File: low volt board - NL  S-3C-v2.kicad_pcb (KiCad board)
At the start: 2 copper layers, 152.4 x 78.7 mm, 42 parts, among them J1 ESP32-S3-ETH-WAVETREE-Footpri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, J2 ILI9341 TFT 2.8" Display with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, J3 4 Channel 5v Relay Connector, J4 SPDT (on)-off-(on), J5 ADC Inputs - 24v side, J6 Dry Contact OptoCoupler, J8 5vIn, Q1-Buzzer1 S8050, SW1 SW_SPDT, U1 ADS1115IDGS - low volt, U2 ADS1115IDGS - 24v, U3-Opto1 PC817

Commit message: Final design before first autoroute
Co-Authored-By: Claude Opus 4.6 <noreply@anthropic.com>
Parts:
- moved J3 38.4 mm to (155.0, 67.0), turned to 90 degrees
- moved J8 37.2 mm to (132.7, 53.3), turned to 90 degrees
- moved J5 27.9 mm to (155.0, 104.0)
- moved R17-A1-3 23.1 mm to (142.8, 78.6)
- moved R18-A1-2 23.0 mm to (142.8, 83.7)
- moved R10-A2-3 22.5 mm to (142.8, 88.7)
- moved R16-A2-0 22.5 mm to (142.8, 104.0)
- moved R8-A2-1 22.5 mm to (142.8, 98.9)
- moved R9-A2-2 22.5 mm to (142.8, 93.8)
- moved R2-Throw-A1 21.2 mm to (89.8, 78.8)
- moved R4-Common1 20.9 mm to (89.8, 73.8)
- moved J4 20.9 mm to (76.8, 78.8)
- moved R3-ThrowB1 20.5 mm to (89.8, 68.7)
- moved R15-Purple1 17.5 mm to (137.6, 101.6)
- moved SW1 17.0 mm to (88.9, 58.4), turned to 90 degrees
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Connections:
- net /IO21 renamed /Buzer-IO21
- net Net-(LS1-Buzzer1--LEAD) renamed /Buzzer-3
- net Net-(Q1-Buzzer1-B) renamed /Buzzer-2
- J3 pad 1: +5V -> /IO3
- J3 pad 2: GND -> /IO15
- J3 pad 3: /IO16 -> /IO18
- J3 pad 4: /IO18 -> /IO16
- J3 pad 5: /IO15 -> GND
- J3 pad 6: /IO3 -> +5V
- J5 pad 6: /A1-2-E -> /A1-3-E
- J8 pad 1: +5V -> GND
- J8 pad 2: GND -> +5V
- R8-A2-1 pad 1: /A2-1 -> /A2-1-E
- R8-A2-1 pad 2: /A2-1-E -> /A2-1
- R9-A2-2 pad 1: /A2-2 -> /A2-2-E
- R9-A2-2 pad 2: /A2-2-E -> /A2-2
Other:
- board size 152.4 x 78.7 mm -> 124.5 x 73.7 mm

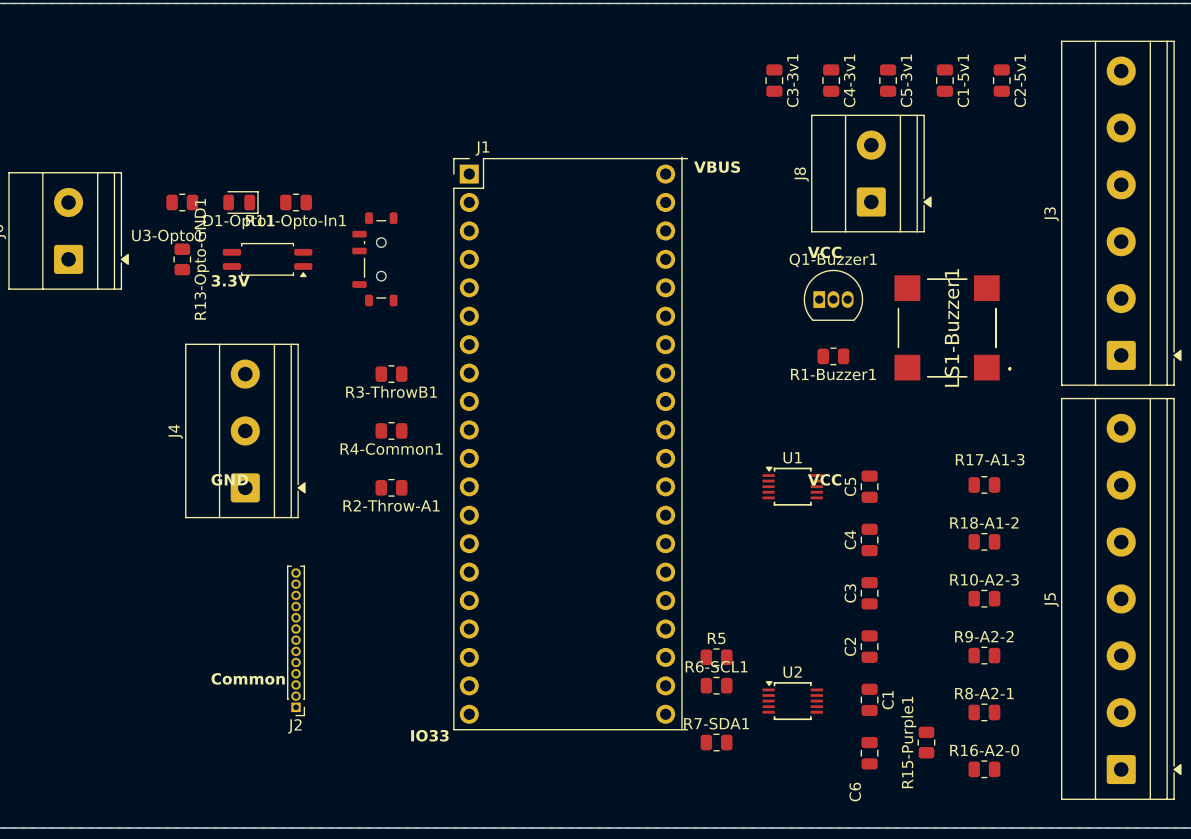
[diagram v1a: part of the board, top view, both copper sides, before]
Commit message: First routing done
Co-Authored-By: Claude Opus 4.6 <noreply@anthropic.com>
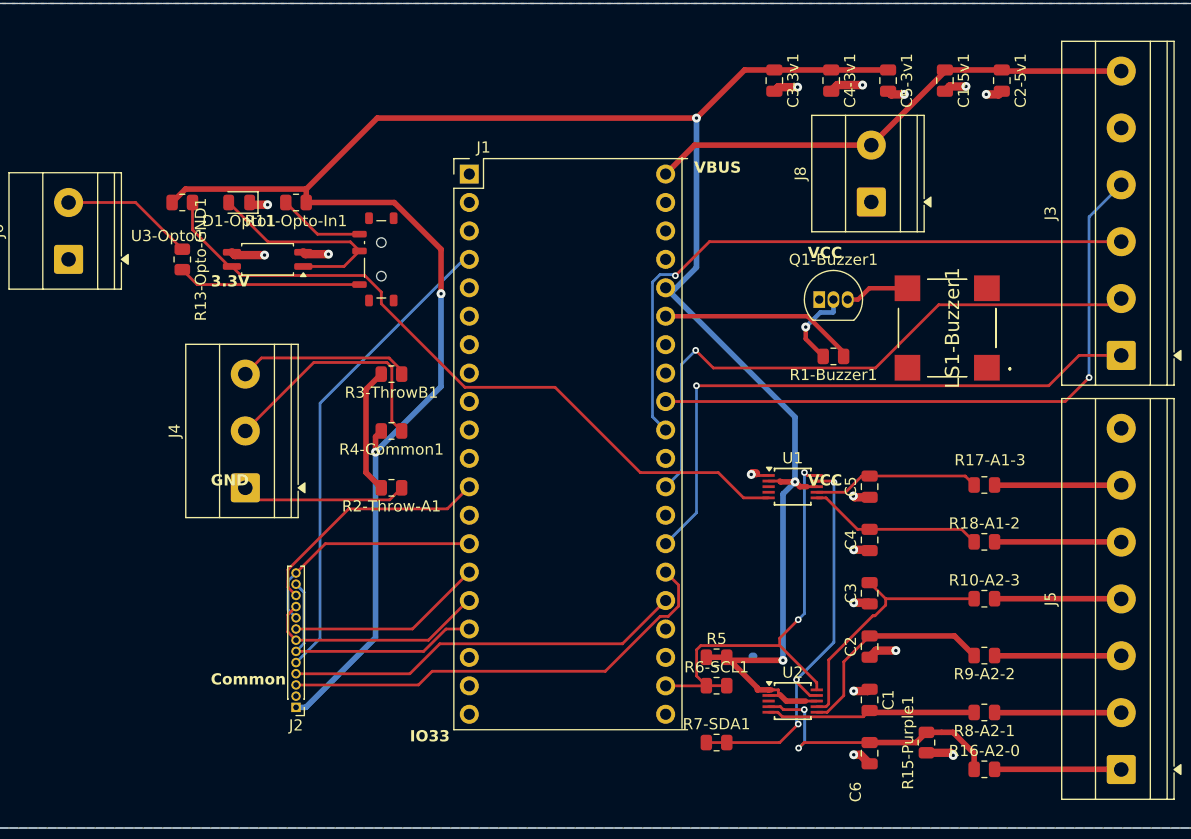
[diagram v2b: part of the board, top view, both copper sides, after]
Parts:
- turned R8-A2-1 to 180 degrees
- turned R9-A2-2 to 180 degrees
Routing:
- net +3.3V: track 0.00 -> 210.3 mm, vias 0 -> 5
- net /A1-1: track 0.00 -> 64.4 mm
- net /IO18: track 0.00 -> 57.1 mm, vias 0 -> 1
- net /IO16: track 0.00 -> 57.1 mm, vias 0 -> 1
- net /IO15: track 0.00 -> 54.5 mm, vias 0 -> 1
- net /IO3: track 0.00 -> 54.3 mm, vias 0 -> 1
- net +5V: track 0.00 -> 44.7 mm
- net /IO48: track 0.00 -> 42.7 mm
- net /IO2: track 0.00 -> 40.6 mm
- net /SCL: track 0.00 -> 39.5 mm, vias 0 -> 2
- net /SDA: track 0.00 -> 36.0 mm, vias 0 -> 3
- net /IO1: track 0.00 -> 35.7 mm
- net GND: track 0.00 -> 31.9 mm, vias 0 -> 16
- net /A2-0: track 0.00 -> 25.4 mm, vias 0 -> 2
- net /IO35: track 0.00 -> 22.9 mm
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
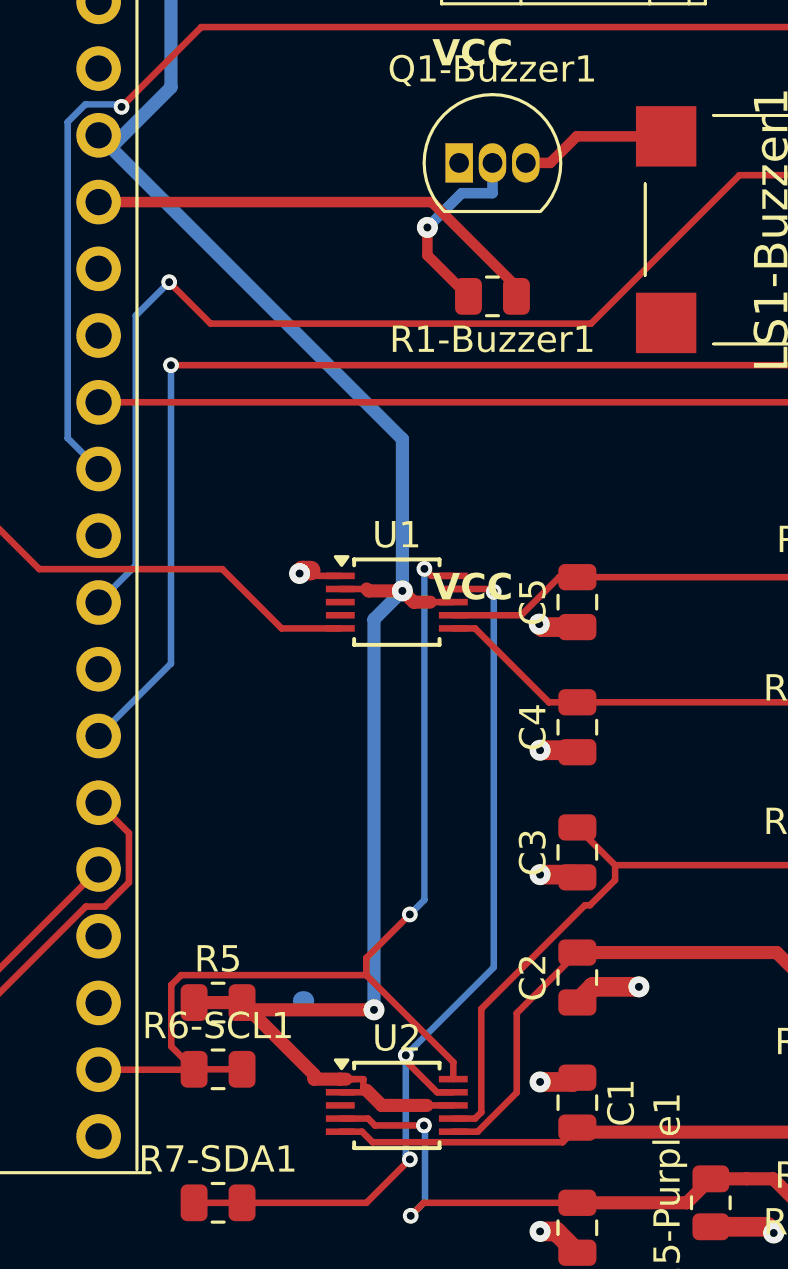
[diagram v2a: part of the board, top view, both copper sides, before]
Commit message: Traces and DRC passing - still need mounting holes
Co-Authored-By: Claude Opus 4.6 <noreply@anthropic.com>
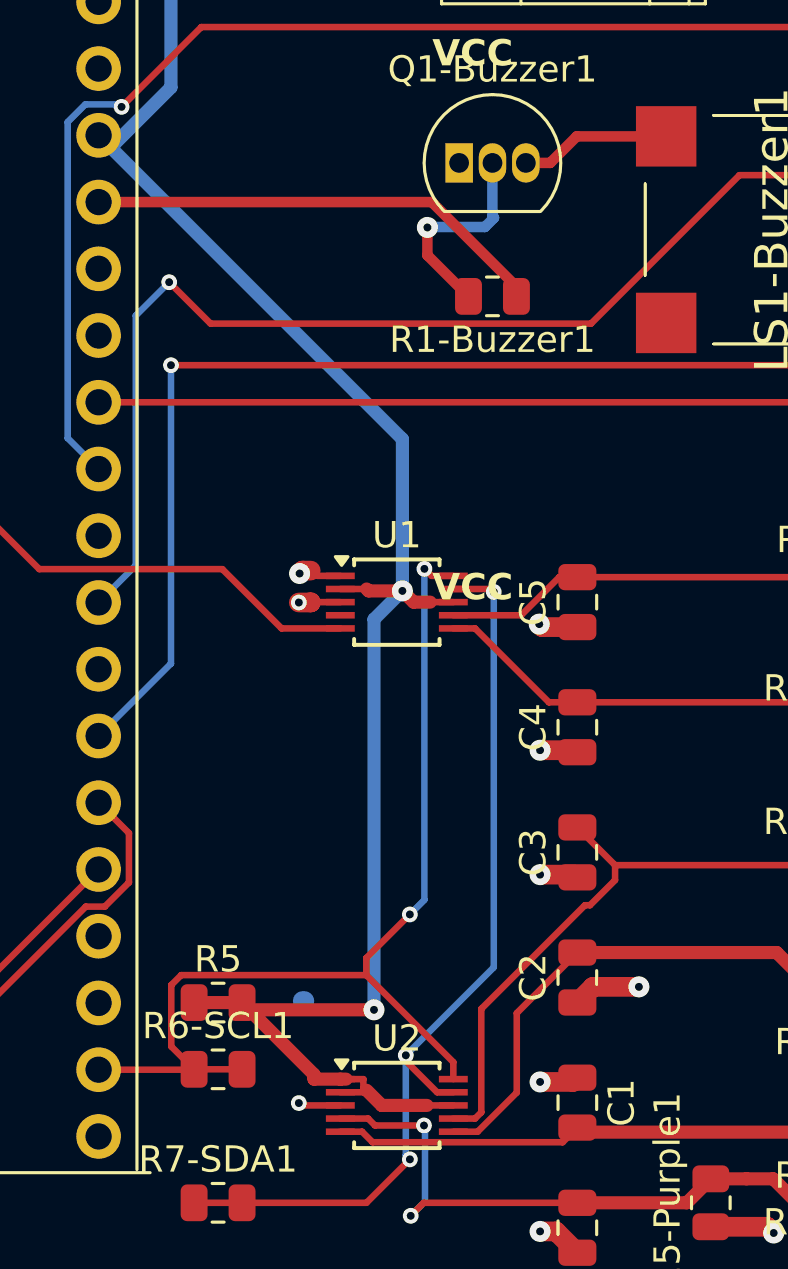
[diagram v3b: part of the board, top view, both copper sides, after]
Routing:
- net GND: track 31.9 -> 35.1 mm, vias 16 -> 18
- net /Buzzer-2: track 7.44 -> 8.07 mm
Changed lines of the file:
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@@
 		(sheetname "/")
 		(sheetfile "low volt board - NL  S-3C-v2.kicad_sch")
+		(clearance 0.15)
 		(attr through_hole)
 		(fp_line
@@
 	)
 	(segment
+		(start 122.374 78.74)
+		(end 122.374 78.726)
+		(width 0.75)
+		(layer "F.Cu")
+		(net 2)
+	)
+	(segment
 		(start 122.0606 77.5258)
 		(end 122.3731 77.5258)
@@
 	)
 	(segment
+		(start 121.92 78.74)
+		(end 122.374 78.74)
+		(width 0.75)
+		(layer "F.Cu")
+		(net 2)
+	)
+	(segment
 		(start 77.3376 53.5401)
 		(end 77.1375 53.34)
@@
 	)
 	(segment
+		(start 122.374 78.726)
+		(end 123.5 78.726)
+		(width 0.25)
+		(layer "F.Cu")
+		(net 2)
+	)
+	(segment
 		(start 141.1295 42.9741)
 		(end 139.6759 42.9741)
@@
 	)
 	(segment
+		(start 121.92 97.79)
+		(end 122.0097 97.8797)
+		(width 0.25)
+		(layer "F.Cu")
+		(net 2)
+	)
+	(segment
+		(start 122.0097 97.8797)
+		(end 123.5 97.8797)
+		(width 0.25)
+		(layer "F.Cu")
+		(net 2)
+	)
+	(segment
 		(start 139.7485 102.4985)
 		(end 137.6 102.4985)
@@
 	)
 	(via
+		(at 121.92 78.74)
+		(size 0.6)
+		(drill 0.3)
+		(layers "F.Cu" "B.Cu")
+		(free yes)
+		(net 2)
+	)
+	(via
 		(at 131.1023 96.9863)
 		(size 0.8)
@@
 	)
 	(via
+		(at 121.92 97.79)
+		(size 0.6)
+		(drill 0.3)
+		(layers "F.Cu" "B.Cu")
+		(free yes)
+		(net 2)
+	)
+	(via
 		(at 131.07 79.5635)
 		(size 0.8)
@@
 	)
 	(segment
-		(start 129.29 62.01)
-		(end 129.29 63.1617)
+		(start 126.8295 64.45)
+		(end 126.8134 64.4661)
 		(width 0.4)
 		(layer "B.Cu")
@@
 	)
 	(segment
-		(start 129.29 63.1617)
-		(end 128.1178 63.1617)
+		(start 129.35 64.1)
+		(end 129 64.45)
 		(width 0.4)
 		(layer "B.Cu")
@@
 	)
 	(segment
-		(start 128.1178 63.1617)
-		(end 126.8134 64.4661)
+		(start 129.29 64.04)
+		(end 129.35 64.1)
+		(width 0.4)
+		(layer "B.Cu")
+		(net 65)
+	)
+	(segment
+		(start 129.29 62.01)
+		(end 129.29 64.04)
+		(width 0.4)
+		(layer "B.Cu")
+		(net 65)
+	)
+	(segment
+		(start 129 64.45)
+		(end 126.8295 64.45)
 		(width 0.4)
 		(layer "B.Cu")

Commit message: Traces and DRC passing - still need mounting holes
Co-Authored-By: Claude Opus 4.6 <noreply@anthropic.com>
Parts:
- added H1: MountingHole, MountingHole:MountingHole_4.3mm_M4_DIN965_Pad, F.Cu at (64.8, 72.4)
- added H2: MountingHole, MountingHole:MountingHole_4.3mm_M4_DIN965_Pad, F.Cu at (166.4, 72.4)
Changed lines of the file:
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@@
 		)
 	)
+	(footprint "MountingHole:MountingHole_4.3mm_M4_DIN965_Pad"
+		(layer "F.Cu")
+		(at 64.77 72.39)
+		(descr "Mounting Hole 4.3mm, M4, generated by kicad-footprint-generator mountinghole.py")
+		(tags "mountinghole M4 DIN965")
+		(property "Reference" "H1"
+			(at 0 -4.7 0)
+			(layer "F.SilkS")
+			(effects
+				(font
+					(size 1 1)
+					(thickness 0.15)
+				)
+			)
+		)
+		(property "Value" "MountingHole"
+			(at 0 4.7 0)
+			(layer "F.Fab")
+			(effects
+				(font
+					(size 1 1)
+					(thickness 0.15)
+				)
+			)
+		)
+		(property "Datasheet" "~"
+			(at 0 0 0)
+			(layer "F.Fab")
+			(hide yes)
+			(effects
+				(font
+					(size 1.27 1.27)
+					(thickness 0.15)
+				)
+			)
+		)
+		(property "Description" "Mounting Hole without connection"
+			(at 0 0 0)
+			(layer "F.Fab")
+			(hide yes)
+			(effects
+				(font
+					(size 1.27 1.27)
+					(thickness 0.15)
+				)
+			)
+		)
+		(property ki_fp_filters "MountingHole*")
+		(sheetname "/")
+		(sheetfile "low volt board - NL  S-3C-v2.kicad_sch")
+		(attr exclude_from_pos_files exclude_from_bom)
+		(fp_circle
+			(center 0 0)
+			(end 3.75 0)
+			(stroke
+				(width 0.15)
+				(type solid)
+			)
+			(fill no)
+			(layer "Cmts.User")
+		)
+		(fp_circle
+			(center 0 0)
+			(end 4 0)
+			(stroke
+				(width 0.05)
+				(type solid)
+			)
+			(fill no)
+			(layer "F.CrtYd")
+		)
+		(fp_text user "${REFERENCE}"
+			(at 0 0 0)
+			(layer "F.Fab")
+			(effects
+				(font
+					(size 1 1)
+					(thickness 0.15)
+				)
+			)
+		)
+		(pad "1" thru_hole circle
+			(at 0 0)
+			(size 7.5 7.5)
+			(drill 4.3)
+			(layers "*.Cu" "*.Mask")
+			(remove_unused_layers no)
+			(zone_connect 2)
+		)
+		(embedded_fonts no)
+	)
 	(footprint "Package_SO:TSSOP-10_3x3mm_P0.5mm"
 		(layer "F.Cu")
@@
 		)
 	)
+	(footprint "MountingHole:MountingHole_4.3mm_M4_DIN965_Pad"
+		(layer "F.Cu")
+		(at 166.37 72.39)
+		(descr "Mounting Hole 4.3mm, M4, generated by kicad-footprint-generator mountinghole.py")
+		(tags "mountinghole M4 DIN965")
+		(property "Reference" "H2"
+			(at 0 -4.7 0)
+			(layer "F.SilkS")
+			(effects
+				(font
+					(size 1 1)
+					(thickness 0.15)
+				)
+			)
+		)
+		(property "Value" "MountingHole"
+			(at 0 4.7 0)
+			(layer "F.Fab")
+			(effects
+				(font
+					(size 1 1)
+					(thickness 0.15)
+				)
+			)
+		)
+		(property "Datasheet" "~"
+			(at 0 0 0)
+			(layer "F.Fab")
+			(hide yes)
+			(effects
+				(font
+					(size 1.27 1.27)
+					(thickness 0.15)
+				)
+			)
+		)
+		(property "Description" "Mounting Hole without connection"
+			(at 0 0 0)
+			(layer "F.Fab")
+			(hide yes)
+			(effects
+				(font
+					(size 1.27 1.27)
+					(thickness 0.15)
+				)
+			)
+		)
+		(property ki_fp_filters "MountingHole*")
+		(sheetname "/")
+		(sheetfile "low volt board - NL  S-3C-v2.kicad_sch")
+		(attr exclude_from_pos_files exclude_from_bom)
+		(fp_circle
+			(center 0 0)
+			(end 3.75 0)
+			(stroke
+				(width 0.15)
+				(type solid)
+			)
+			(fill no)
+			(layer "Cmts.User")
+		)
+		(fp_circle
+			(center 0 0)
+			(end 4 0)
+			(stroke
+				(width 0.05)
+				(type solid)
+			)
+			(fill no)
+			(layer "F.CrtYd")
+		)
+		(fp_text user "${REFERENCE}"
+			(at 0 0 0)
+			(layer "F.Fab")
+			(effects
+				(font
+					(size 1 1)
+					(thickness 0.15)
+				)
+			)
+		)
+		(pad "1" thru_hole circle
+			(at 0 0)
+			(size 7.5 7.5)
+			(drill 4.3)
+			(layers "*.Cu" "*.Mask")
+			(remove_unused_layers no)
+			(zone_connect 2)
+		)
+		(embedded_fonts no)
+	)
 	(footprint "Resistor_SMD:R_0805_2012Metric"

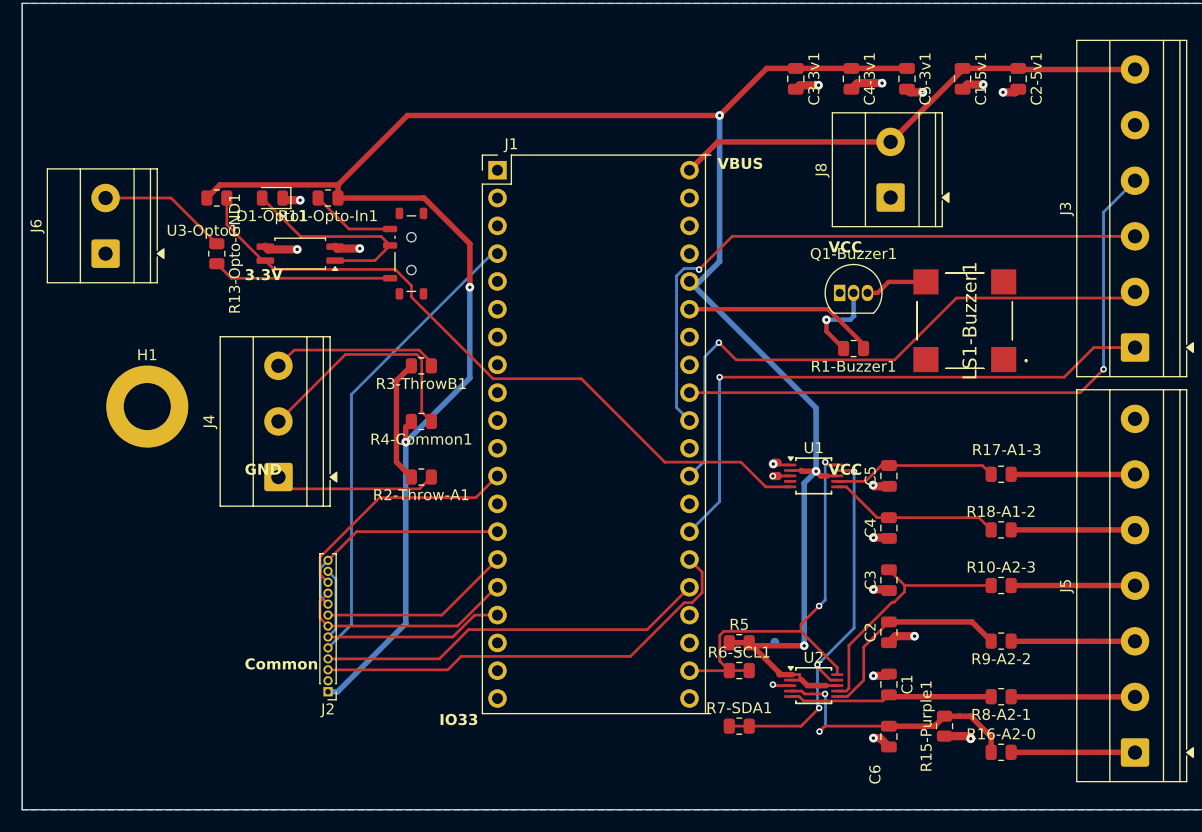
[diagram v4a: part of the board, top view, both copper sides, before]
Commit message: Fixed footprint issues
Co-Authored-By: Claude Opus 4.6 <noreply@anthropic.com>
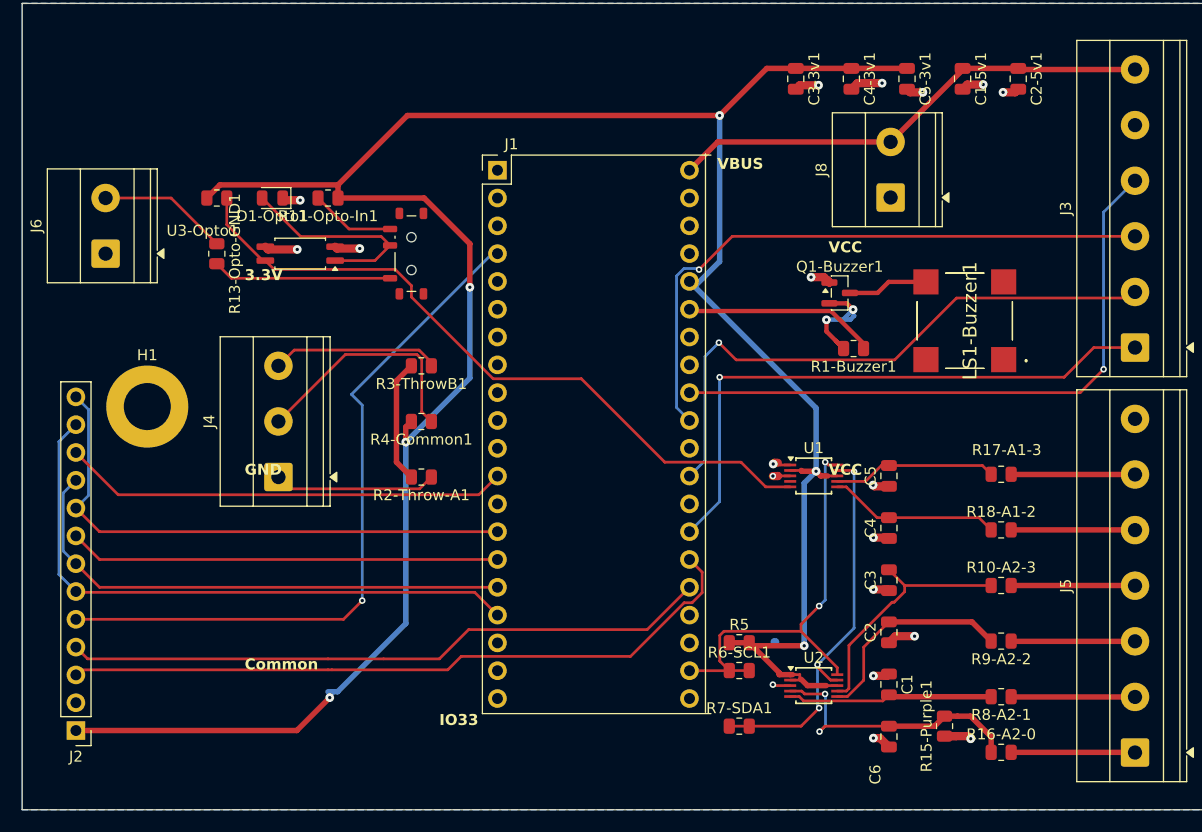
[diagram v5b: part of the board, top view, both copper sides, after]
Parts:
- J2: footprint Connector_PinHeader_1.00mm:PinHeader_1x13_P1.00mm_Vertical -> Connector_PinHeader_2.54mm:PinHeader_1x13_P2.54mm_Vertical
- Q1-Buzzer1: footprint Package_TO_SOT_THT:TO-92_Inline -> Package_TO_SOT_SMD:SOT-23
- moved J2 23.3 mm to (58.2, 102.0)
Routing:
- net /IO35: track 22.9 -> 55.9 mm
- net /IO38 (SDO): track 21.2 -> 50.5 mm
- net /IO36: track 20.6 -> 48.0 mm
- net +3.3V: track 210.3 -> 235.3 mm, vias 5 -> 6
- net /IO1: track 35.7 -> 59.2 mm
- net /IO2: track 40.6 -> 63.8 mm
- net /IO48: track 42.7 -> 64.8 mm, vias 0 -> 1
- net /IO37: track 17.6 -> 39.4 mm
- net /IO39: track 21.9 -> 40.8 mm
- net GND: track 35.1 -> 38.3 mm, vias 18 -> 19
- net /Buzzer-2: track 8.07 -> 10.7 mm, vias 1 -> 2
- net /Buzzer-3: track 5.76 -> 7.36 mm
- net /A2-0: track 25.4 -> 26.6 mm
